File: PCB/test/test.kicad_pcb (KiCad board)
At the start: 2 copper layers, 40.2 x 30 mm, 106 parts, among them CN5 UFL, SW2 MLL1200S_TE, U1 STM32WBxx_QFN48, U2 USBLC6-2SC6, U3 LD3985M33R, X1 NX2016_32MHz, X2 NX2012_32K768Hz

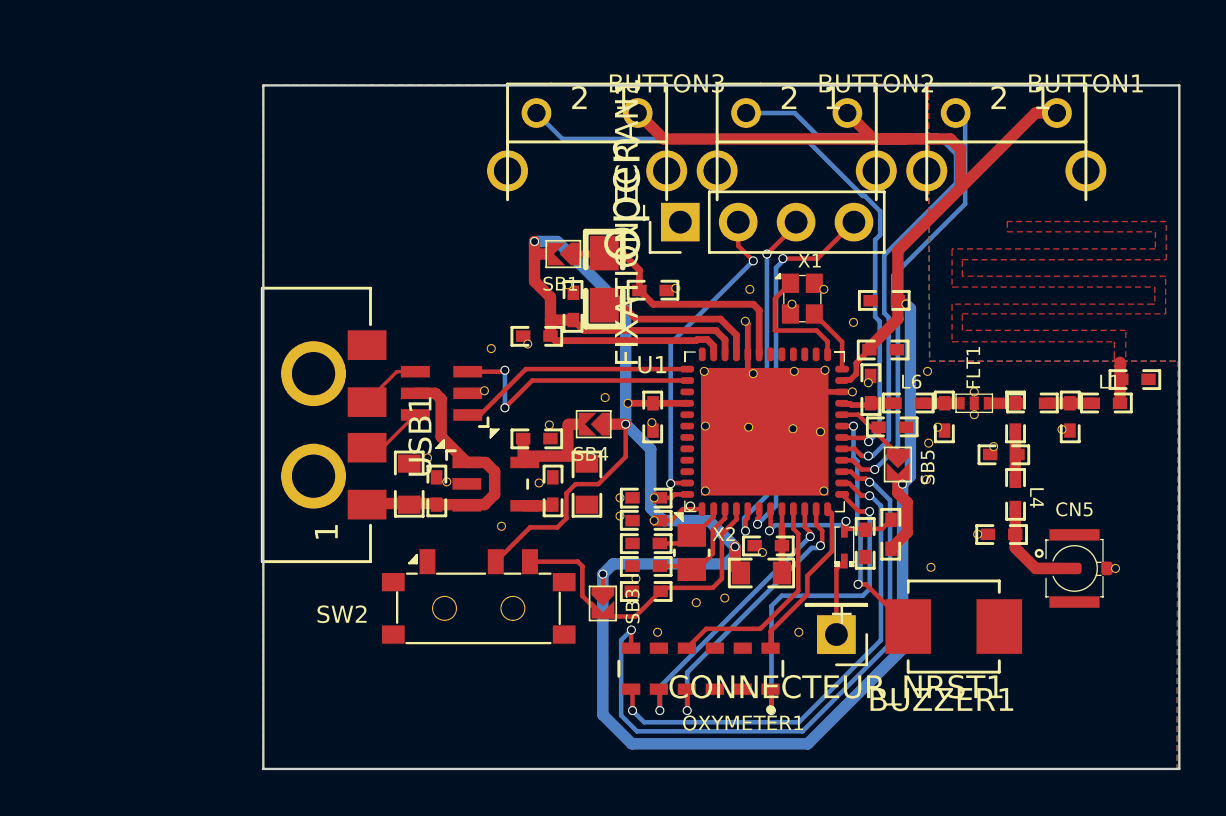
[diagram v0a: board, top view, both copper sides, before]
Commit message: suppression du bouton boot + pcb usb
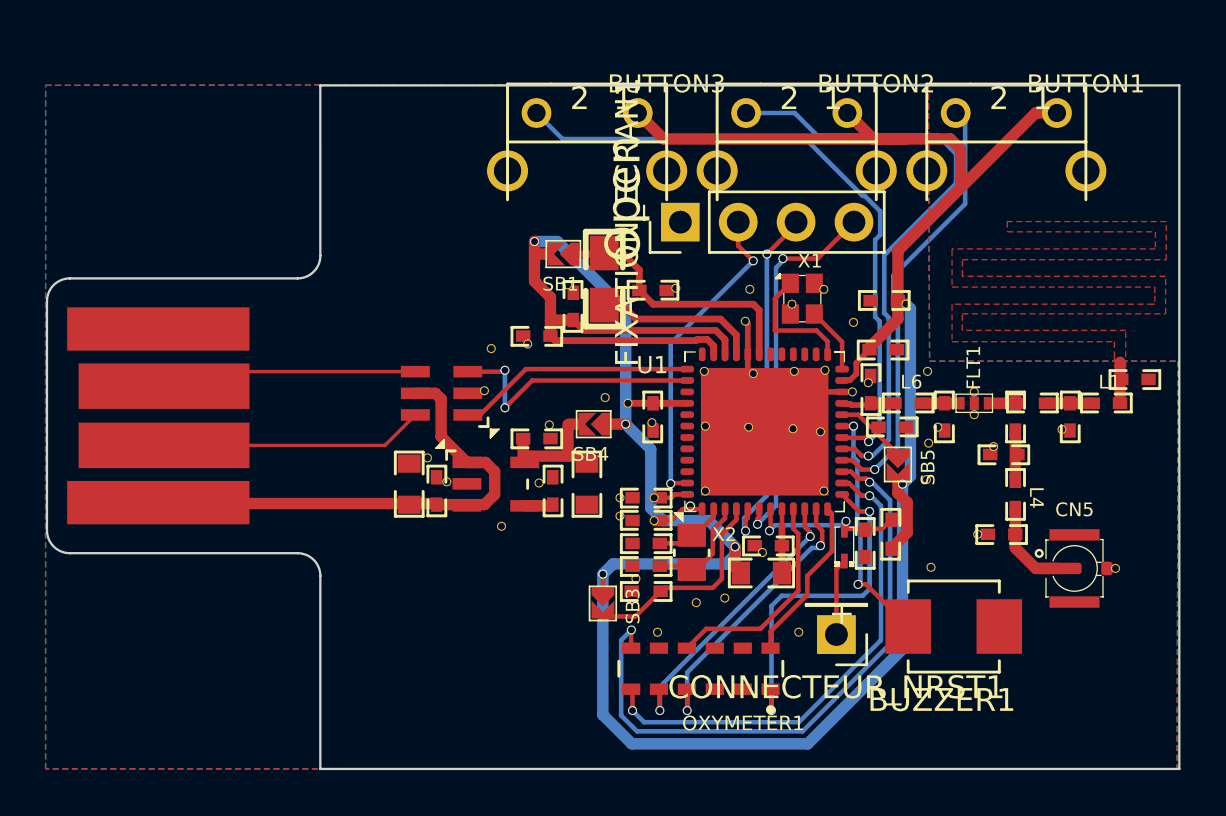
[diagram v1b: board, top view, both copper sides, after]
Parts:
- removed SW2: MLL1200S_TE, Library:MLL1200S_TE
- USB1: value 629004113921 -> USB_A_PLUG; footprint 629004113921:629004113921 -> Connector_USB:usb-PCB
- moved USB1 11.7 mm to (103.5, 92.4)
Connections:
- net BOOT0 renamed Net-(R2-Pad1)
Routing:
- net 3V3: track 141.7 -> 132.0 mm
- net 5V_USB: track 12.7 -> 21.9 mm
- net Net-(U2-Pad6): track 2.67 -> 11.6 mm
- net Net-(U2-Pad4): track 2.63 -> 11.3 mm
- net Net-(R2-Pad1): track 14.2 -> 9.23 mm
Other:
- board size 40.2 x 30 mm -> 49.7 x 30 mm

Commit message: changement oxymètre
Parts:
- removed OXYMETER1: SFH_7060, SFH_7060:XDCR_SFH_7060
- added ?: , , F.Cu at (135.0, 101.6)
- added ?: , , F.Cu at (130.8, 103.6)
- added OXY1: SFH_7072, SFH_7060:XDCR_SFH_7060, F.Cu at (132.2, 103.6)
- moved USB1 5.70 mm to (109.2, 92.4)
- moved ? 0.28 mm to (130.1, 101.7)
- moved ? 0.11 mm to (133.2, 100.3)
- moved ? 0.10 mm to (132.0, 100.5)
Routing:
- net Net-(U2-Pad6): track 11.6 -> 5.89 mm
- net 5V_USB: track 21.9 -> 16.2 mm
- net PA6: track 27.4 -> 21.7 mm
- net Net-(U2-Pad4): track 11.3 -> 6.50 mm
- net PA2: track 12.5 -> 7.92 mm
- net PA1: track 12.6 -> 8.04 mm
- net PA5: track 21.6 -> 18.2 mm
- net PA3: track 7.29 -> 10.6 mm
- net PA4: track 15.1 -> 13.1 mm
- net PA0: track 9.60 -> 10.9 mm
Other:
- board size 49.7 x 30 mm -> 44 x 30 mm

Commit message: beaucoup de changements
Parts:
- removed the ? at (144.3, 97.6)
- removed the ? at (142.3, 99.0)
- removed the ? at (135.0, 101.6)
- removed the ? at (136.5, 101.9)
- removed the ? at (142.1, 95.2)
- removed the ? at (139.6, 91.0)
- removed the ? at (130.1, 101.7)
- removed the ? at (134.2, 88.2)
- removed the ? at (138.9, 88.3)
- removed the ? at (123.0, 89.5)
- removed the ? at (141.2, 87.5)
- removed the ? at (145.1, 93.8)
- removed the ? at (142.2, 93.6)
- removed the ? at (150.4, 99.1)
- removed the ? at (132.0, 100.5)
- removed the ? at (123.5, 97.2)
- removed the ? at (134.3, 86.8)
- removed BUTTON1, BUTTON2, BUTTON3: 9-1437565-9, 9-1437565-9:FSMRACD
- removed BUZZER1: CMT-4023S-SMT-TR, CMT-4023S-SMT-TR:CUI_CMT-4023S-SMT-TR
- removed C28, C29, C8: NF, Library:0402_CAP_NPOL
- removed CN5: UFL, Library:UFL
- removed L4: 0R, Library:0402_COIL
- removed SB3: Open, Library:SB-tiny
- added ?: , , F.Cu at (151.1, 122.6)
- added ?: , , F.Cu at (138.4, 87.8)
- added ?: , , F.Cu at (141.5, 122.6)
- added ?: , , F.Cu at (135.3, 100.5)
- added ?: , , F.Cu at (129.0, 94.3)
- added ?: , , F.Cu at (139.1, 122.6)
- added ?: , , F.Cu at (136.7, 122.6)
- added ?: , , F.Cu at (130.3, 122.6)
- added ?: , , F.Cu at (135.6, 127.8)
- added ?: , , F.Cu at (140.7, 122.6)
- added ?: , , F.Cu at (145.5, 122.6)
- added ?: , , F.Cu at (126.8, 125.7)
- added ?: , , F.Cu at (127.1, 122.6)
- added ?: , , F.Cu at (134.1, 88.3)
- added ?: , , F.Cu at (127.9, 122.6)
- added ?: , , F.Cu at (147.1, 122.6)
- added ?: , , F.Cu at (140.9, 92.7)
- added ?: , , F.Cu at (150.3, 122.6)
- added ?: , , F.Cu at (137.3, 125.3)
- added ?: , , F.Cu at (138.2, 100.4)
- added ?: , , F.Cu at (144.7, 122.6)
- added ?: , , F.Cu at (142.3, 122.6)
- added ?: , , F.Cu at (128.0, 89.2)
- added ?: , , F.Cu at (141.0, 102.9)
- added ?: , , F.Cu at (143.1, 122.6)
- added ?: , , F.Cu at (129.5, 122.6)
- added ?: , , F.Cu at (133.5, 122.6)
- added ?: , , F.Cu at (143.9, 122.6)
- added ?: , , F.Cu at (148.7, 122.6)
- added ?: , , F.Cu at (128.9, 100.6)
- added ?: , , F.Cu at (143.4, 96.2)
- added ?: , , F.Cu at (135.4, 104.0)
- added ?: , , F.Cu at (136.4, 95.6)
- added ?: , , F.Cu at (137.5, 122.6)
- added ?: , , F.Cu at (135.9, 122.6)
- added ?: , , F.Cu at (144.0, 94.5)
- added ?: , , F.Cu at (126.9, 95.4)
- added ?: , , F.Cu at (125.0, 98.3)
- added ?: , , F.Cu at (138.3, 122.6)
- added ?: , , F.Cu at (134.2, 95.6)
- added ?: , , F.Cu at (126.3, 122.6)
- added ?: , , F.Cu at (147.9, 122.6)
- added ?: , , F.Cu at (139.4, 99.0)
- added ?: , , F.Cu at (146.3, 122.6)
- added ?: , , F.Cu at (139.9, 122.6)
- added ?: , , F.Cu at (124.7, 122.6)
- added ?: , , F.Cu at (135.1, 122.6)
- added ?: , , F.Cu at (132.7, 122.6)
- added ?: , , F.Cu at (140.6, 91.0)
- added ?: , , F.Cu at (128.7, 122.6)
- added ?: , , F.Cu at (149.5, 122.6)
- added ?: , , F.Cu at (134.3, 122.6)
- added ?: , , F.Cu at (131.1, 122.6)
- added ?: , , F.Cu at (125.5, 122.6)
- added ?: , , F.Cu at (131.9, 122.6)
- added BATTERY: BAT-HLD-002-SMT, BAT-HLD-002-SMT:BAT_BAT-HLD-002-SMT, F.Cu at (138.0, 155.8)
- added BT: Conn_01x02_Male, Connector_PinHeader_2.54mm:PinHeader_1x02_P2.54mm_Vertical, F.Cu at (132.3, 102.0)
- added BUZZER: KSSG13J12-N, KSSG13J12-N:XDCR_KSSG13J12-N, F.Cu at (148.3, 96.9)
- added JOYSTICK: JS1400AFQ, JS1400AFQ:SW_JS1400AFQ, F.Cu at (132.0, 116.4)
- C1, C2: footprint Library:0402_CAP_NPOL -> Passive.PcbLib:0402_CAP_NPOL
- moved ? 24.6 mm to (131.1, 128.2)
- moved OXY 24.6 mm to (132.5, 128.2)
- moved C23 10.1 mm to (126.9, 102.2), turned to 0 degrees
- moved NRST 9.25 mm to (147.4, 102.0)
- moved ? 9.06 mm to (125.8, 101.4), turned to 90 degrees
- moved C24 8.47 mm to (127.2, 101.0), turned to 0 degrees
- moved ? 7.80 mm to (126.8, 100.5), turned to 90 degrees
- moved U3 4.77 mm to (126.9, 98.4), turned to 90 degrees
- moved ? 4.41 mm to (128.6, 87.4)
- moved I2C 4.00 mm to (128.1, 81.5)
- moved L2 3.85 mm to (131.8, 85.0)
- moved ? 3.85 mm to (130.2, 86.4)
- moved C10 3.85 mm to (133.9, 86.7)
- moved C16 3.85 mm to (128.8, 88.7)
- moved C9 3.85 mm to (130.4, 87.4)
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- renumbered FIXATION_ECRAN1 to I2C, CONNECTEUR_NRST1 to NRST, OXY1 to OXY
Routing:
- net 5V_USB: track 16.2 -> 136.2 mm, vias 0 -> 5
- net PA5: track 18.2 -> 58.9 mm
- net PA4: track 13.1 -> 53.0 mm
- net PA6: track 21.7 -> 61.5 mm
- net PA2: track 7.92 -> 44.8 mm
- net PA1: track 8.04 -> 44.0 mm
- net PA3: track 10.6 -> 44.3 mm
- net PA0: track 10.9 -> 43.3 mm
- net 3V3: track 131.7 -> 99.6 mm, vias 5 -> 7
- net PA7: track 19.3 -> 27.1 mm, vias 1 -> 2
- net NRST: track 3.37 -> 10.7 mm
- net Net-(FIXATION_ECRAN1-Pad2): track 14.0 -> 18.8 mm
- net Net-(C29-Pad1): track 4.04 -> 0.00 mm
- net Net-(C10-Pad1): track 11.7 -> 7.72 mm
- net Net-(L2-Pad2): track 7.19 -> 3.45 mm
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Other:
- board size 44 x 30 mm -> 41.6 x 86.8 mm

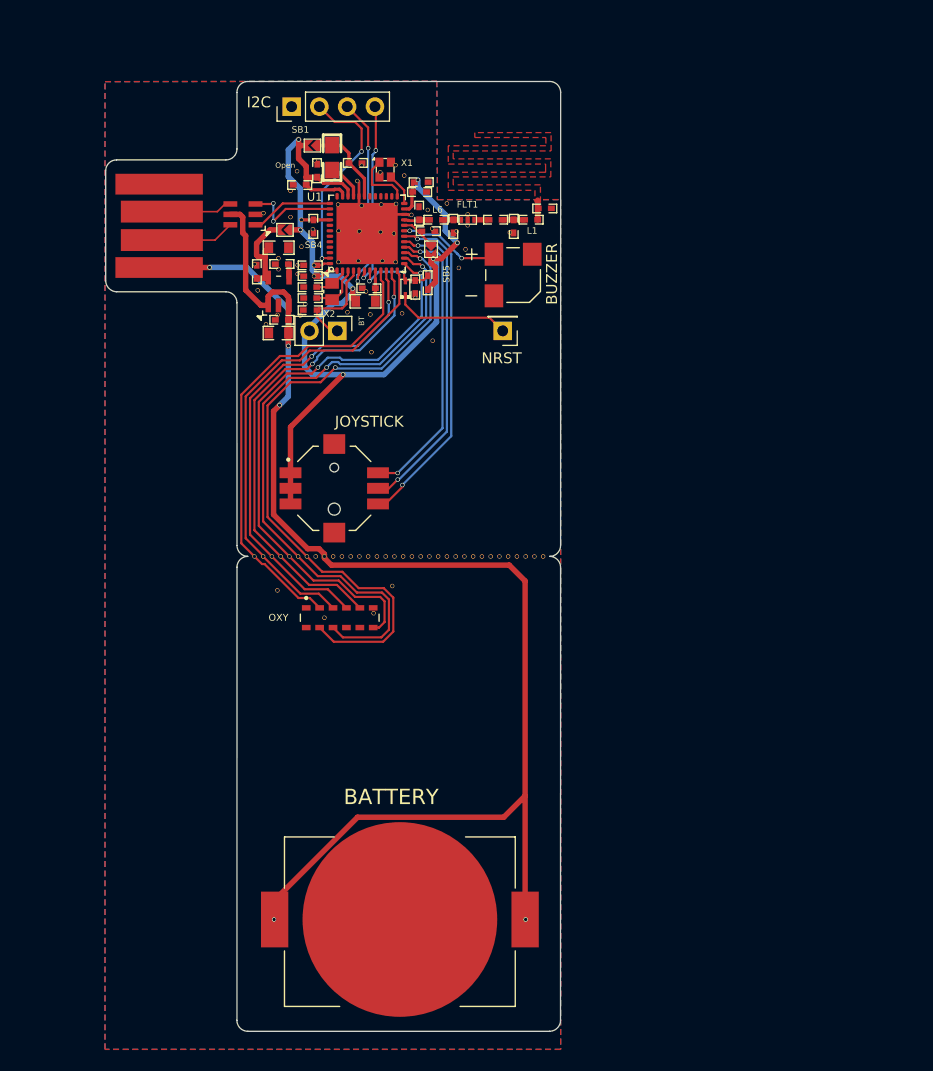
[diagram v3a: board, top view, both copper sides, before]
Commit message: ajout ampliop capteur, reste UVNC et 10x pin header
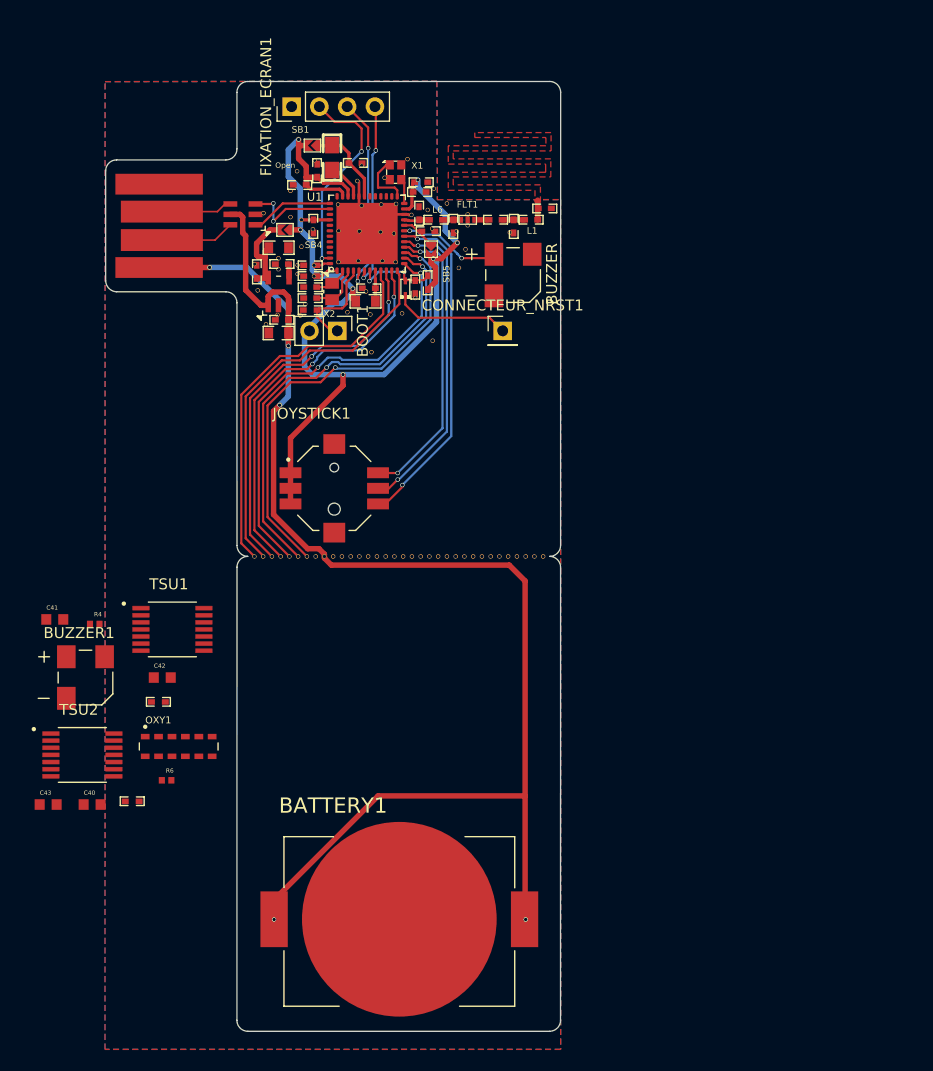
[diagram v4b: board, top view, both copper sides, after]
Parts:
- removed the ? at (138.4, 87.8)
- removed the ? at (135.6, 127.8)
- removed the ? at (126.8, 125.7)
- removed the ? at (137.3, 125.3)
- removed the ? at (136.2, 87.5)
- removed the ? at (131.1, 128.2)
- removed BATTERY: BAT-HLD-002-SMT, BAT-HLD-002-SMT:BAT_BAT-HLD-002-SMT
- removed BT: Conn_01x02_Male, Connector_PinHeader_2.54mm:PinHeader_1x02_P2.54mm_Vertical
- removed I2C: HEADER_1X41, Connector_PinHeader_2.54mm:PinHeader_1x04_P2.54mm_Vertical
- removed JOYSTICK: JS1400AFQ, JS1400AFQ:SW_JS1400AFQ
- removed NRST: Conn_01x01_Female, Connector_PinHeader_2.54mm:PinHeader_1x01_P2.54mm_Vertical
- removed OXY: SFH_7072, SFH_7060:XDCR_SFH_7060
- added ?: , , F.Cu at (141.1, 89.0)
- added ?: , , F.Cu at (136.6, 88.0)
- added BATTERY1: BAT-HLD-002-SMT, BAT-HLD-002-SMT:BAT_BAT-HLD-002-SMT, F.Cu at (137.9, 155.8)
- added BOOT1: Conn_01x02_Male, Connector_PinHeader_2.54mm:PinHeader_1x02_P2.54mm_Vertical, F.Cu at (132.3, 102.0)
- added BUZZER1: KSSG13J12-N, KSSG13J12-N:XDCR_KSSG13J12-N, F.Cu at (109.3, 133.7)
- added C40: C0603C101K5RACTU, C0603C101K5RACTU:CAPC1608X87N, F.Cu at (109.9, 145.3)
- added C41: C0603C101K5RACTU, C0603C101K5RACTU:CAPC1608X87N, F.Cu at (106.4, 128.4)
- added C42: C0603C101K5RACTU, C0603C101K5RACTU:CAPC1608X87N, F.Cu at (116.3, 133.7)
- added C43: C0603C101K5RACTU, C0603C101K5RACTU:CAPC1608X87N, F.Cu at (105.8, 145.3)
- added CONNECTEUR_NRST1: Conn_01x01_Female, Connector_PinHeader_2.54mm:PinHeader_1x01_P2.54mm_Vertical, F.Cu at (147.4, 102.0)
- added FIXATION_ECRAN1: HEADER_1X41, Connector_PinHeader_2.54mm:PinHeader_1x04_P2.54mm_Vertical, F.Cu at (128.1, 81.5)
- added JOYSTICK1: JS1400AFQ, JS1400AFQ:SW_JS1400AFQ, F.Cu at (132.0, 116.4)
- added OXY1: SFH_7072, SFH_7060:XDCR_SFH_7060, F.Cu at (117.8, 140.0)
- added R3: 10K, Library:0402_RES, F.Cu at (115.9, 135.9)
- added R4: CR0402-FX-4700GLF, CR0402-FX-4700GLF:RESC1005X40N, F.Cu at (110.1, 128.8)
- added R5: 10K, Library:0402_RES, F.Cu at (113.5, 145.0)
- added R6: CR0402-FX-4700GLF, CR0402-FX-4700GLF:RESC1005X40N, F.Cu at (116.7, 143.1)
- added TSU1: TSU104IPT, TSU104IPT:SOP65P640X120-14N, F.Cu at (117.2, 129.3)
- added TSU2: TSU104IPT, TSU104IPT:SOP65P640X120-14N, F.Cu at (109.0, 140.8)
- C1, C2: footprint Passive.PcbLib:0402_CAP_NPOL -> Library:0402_CAP_NPOL
- moved ? 1.23 mm to (138.7, 86.3)
- moved X1 0.98 mm to (137.6, 87.5)
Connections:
- U1 pad 15: PA6 -> unconnected-(U1-Pad15)
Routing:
- net PA6: track 61.5 -> 41.3 mm, vias 2 -> 0
- net PA5: track 58.9 -> 40.4 mm
- net PA4: track 53.0 -> 39.4 mm
- net PA2: track 44.8 -> 35.6 mm
- net PA1: track 44.0 -> 35.3 mm
- net PA3: track 44.3 -> 36.0 mm
- net PA0: track 43.3 -> 35.4 mm
- net Net-(U1-Pad24): track 2.92 -> 2.29 mm
- net unconnected-(U1-Pad15): vias 0 -> 2

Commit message: ajout headers, reste circuit + UVNC
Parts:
- removed the ? at (139.1, 122.6)
- removed the ? at (127.1, 122.6)
- removed the ? at (130.3, 122.6)
- removed the ? at (127.9, 122.6)
- removed the ? at (138.2, 100.4)
- removed the ? at (144.7, 122.6)
- removed the ? at (141.0, 102.9)
- removed the ? at (129.5, 122.6)
- removed the ? at (133.5, 122.6)
- removed the ? at (143.4, 96.2)
- removed the ? at (135.4, 104.0)
- removed the ? at (144.0, 94.5)
- removed the ? at (126.3, 122.6)
- removed the ? at (124.7, 122.6)
- removed the ? at (128.7, 122.6)
- removed the ? at (125.5, 122.6)
- removed BUZZER: KSSG13J12-N, KSSG13J12-N:XDCR_KSSG13J12-N
- added ?: , , F.Cu at (146.3, 102.2)
- added ?: , , F.Cu at (127.7, 122.6)
- added ?: , , F.Cu at (137.0, 105.6)
- added ?: , , F.Cu at (125.0, 122.6)
- added ?: , , F.Cu at (144.2, 93.9)
- added ?: , , F.Cu at (148.5, 101.8)
- added ?: , , F.Cu at (149.5, 95.9)
- added ?: , , F.Cu at (139.5, 110.1)
- added ?: , , F.Cu at (139.4, 107.2)
- added ?: , , F.Cu at (130.4, 122.6)
- added ?: , , F.Cu at (143.1, 97.8)
- added ?: , , F.Cu at (129.5, 122.6)
- added ?: , , F.Cu at (143.1, 100.3)
- added ?: , , F.Cu at (126.8, 122.6)
- added ?: , , F.Cu at (141.9, 103.0)
- added ?: , , F.Cu at (144.2, 102.6)
- added ?: , , F.Cu at (134.1, 102.8)
- added ?: , , F.Cu at (128.6, 122.6)
- added ?: , , F.Cu at (125.9, 122.6)
- added ?: , , F.Cu at (140.6, 104.1)
- added ?: , , F.Cu at (137.9, 102.2)
- added HEADER1: 1-146285-0, 1-146285-0:TE_1-146285-0, F.Cu at (150.7, 97.7)
- added HEADER2: 1-146285-0, 1-146285-0:TE_1-146285-0, F.Cu at (150.7, 147.5)
- moved BUZZER1 51.6 mm to (146.1, 97.6)
- moved C43 23.9 mm to (125.2, 131.2), turned to 90 degrees
- moved C41 22.9 mm to (125.1, 141.6), turned to 90 degrees
- moved TSU2 21.8 mm to (128.9, 131.8), turned to 90 degrees
- moved R5 20.5 mm to (125.5, 128.3), turned to 90 degrees
- moved C40 19.4 mm to (127.6, 137.5)
- moved OXY1 19.1 mm to (136.7, 142.9), turned to 90 degrees
- moved TSU1 17.5 mm to (128.8, 142.3), turned to 90 degrees
- moved R4 17.5 mm to (124.3, 138.9), turned to -90 degrees
- moved R6 16.5 mm to (124.4, 128.5), turned to -90 degrees
- moved C42 13.2 mm to (127.7, 127.0)
- moved CONNECTEUR_NRST1 11.5 mm to (135.9, 102.0)
- moved R3 9.89 mm to (125.4, 138.7), turned to 90 degrees
- moved BATTERY1 1.35 mm to (136.8, 156.5)
- moved ? 0.70 mm to (144.8, 122.6)
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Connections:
- ? pad 1: GND -> PA4
- ? pad 1: GND -> PA2
- ? pad 1: GND -> 5V_USB
- ? pad 1: GND -> PA5
- ? pad 1: GND -> PA0
- ? pad 1: GND -> PA3
- ? pad 1: GND -> PA1
- ? pad 1: 5V_USB -> GND
- ? pad 1: GND -> 3V3
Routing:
- net 3V3: track 99.5 -> 170.6 mm
- net 5V_USB: track 136.3 -> 73.0 mm, vias 5 -> 2
- net PA6: track 41.3 -> 0.00 mm
- net PA5: track 40.4 -> 62.9 mm
- net PA4: track 39.4 -> 58.1 mm
- net PA3: track 36.0 -> 52.9 mm
- net PA2: track 35.6 -> 48.7 mm, vias 2 -> 0
- net PA1: track 35.3 -> 44.4 mm, vias 2 -> 0
- net NRST: track 10.7 -> 4.80 mm, vias 0 -> 1
- net PA0: track 35.4 -> 41.2 mm
- net PB2: track 9.38 -> 7.48 mm
- net unconnected-(U1-Pad15): vias 2 -> 0
